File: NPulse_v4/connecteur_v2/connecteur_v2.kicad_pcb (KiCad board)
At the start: 4 copper layers, 39.8 x 51 mm, 26 parts, among them J1 Conn_01x02_Socket, J10 Conn_02x05_Odd_Even, J13 Conn_02x05_Odd_Even, J2 Conn_01x02_Socket, J23 Conn_01x01, J24 Conn_01x06_Socket, J25 Conn_01x06_Socket, J26 Conn_01x06_Socket, J27 Conn_01x01, J28 Conn_01x06_Socket, J29 Conn_01x06_Socket, J3 Conn_01x02_Socket, J30 Conn_01x06_Socket, J31 Conn_01x06_Socket, J32 Conn_02x05_Odd_Even, J33 Conn_01x06_Socket, J35 Conn_02x05_Odd_Even, J4 Conn_01x02_Socket, J45 Conn_01x01, J5 Conn_01x02_Socket, J54 Conn_02x05_Odd_Even, J57 Conn_02x05_Odd_Even, J6 Conn_01x04_Socket

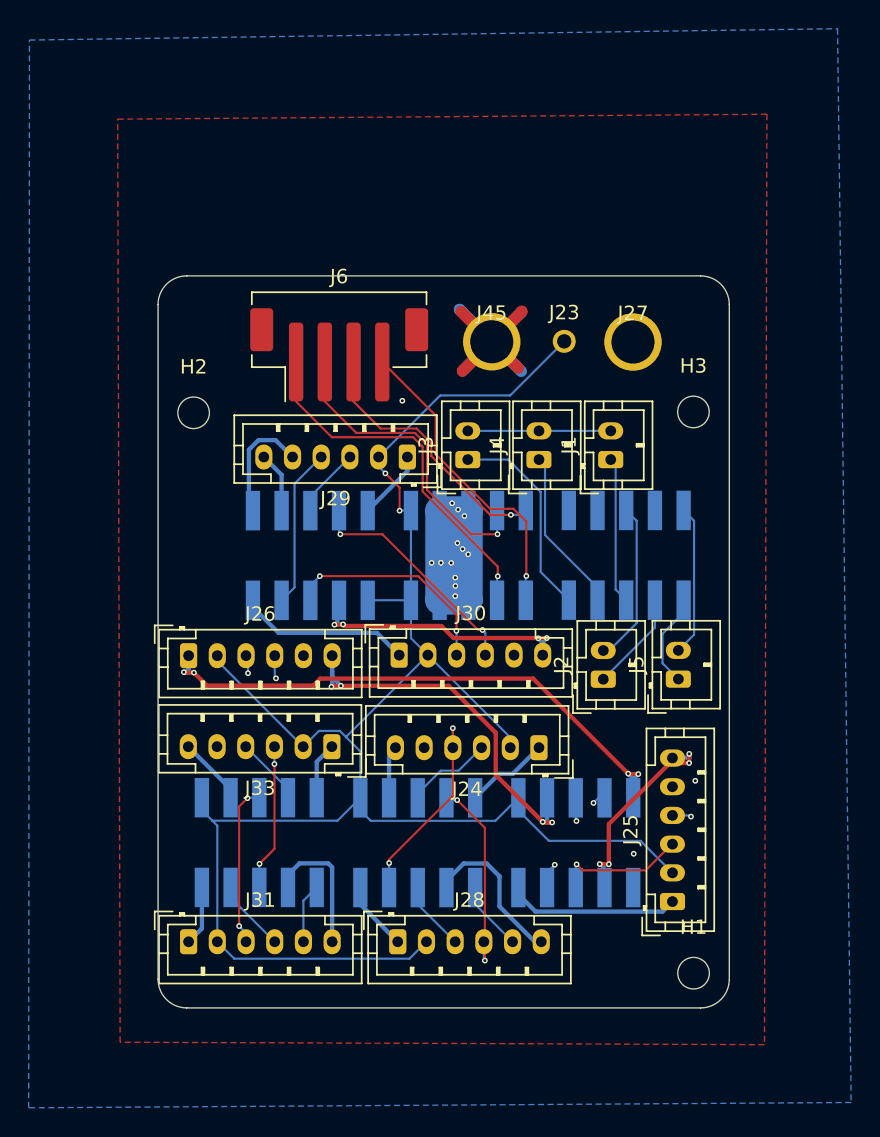
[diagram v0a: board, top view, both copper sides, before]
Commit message: add text on hat board, generate gerbers
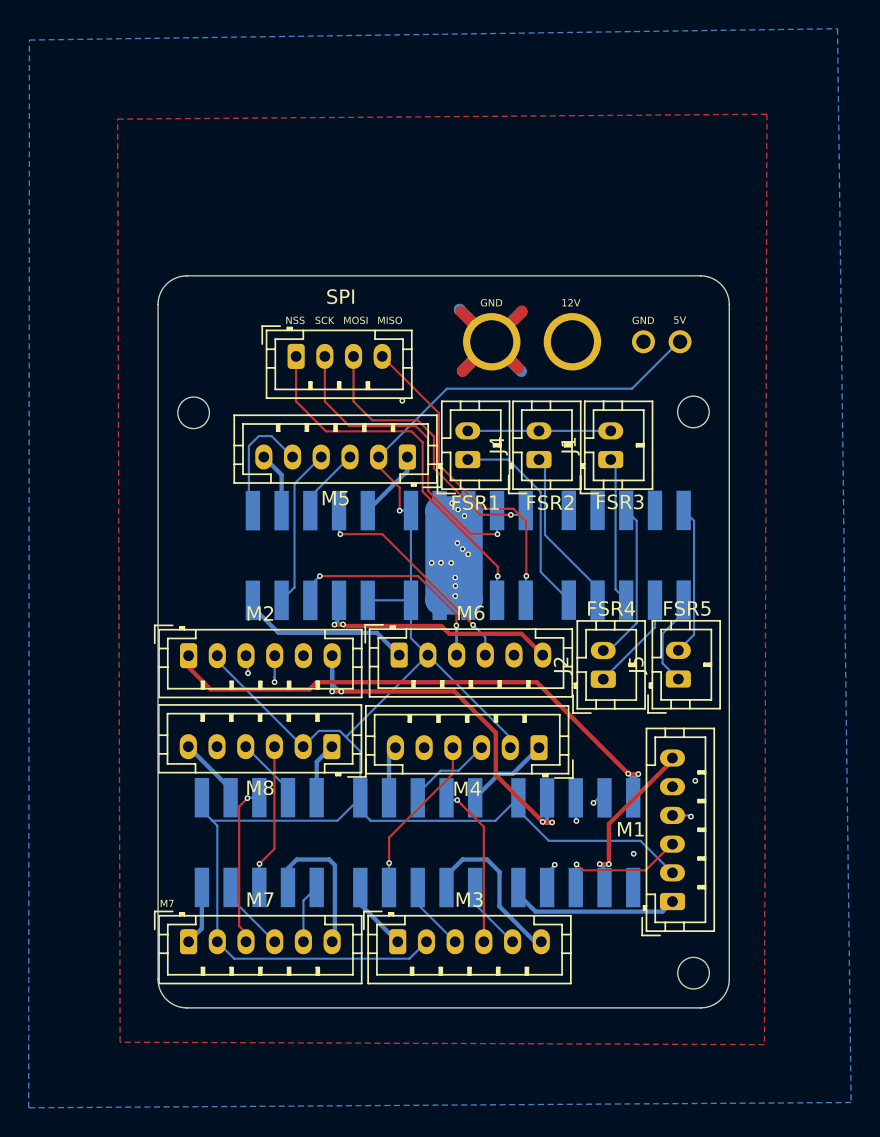
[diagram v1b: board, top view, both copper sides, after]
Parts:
- added ?: , , F.Cu at (187.2, 91.2)
- J6: footprint Connector_JST:JST_PH_B4B-PH-SM4-TB_1x04-1MP_P2.00mm_Vertical -> Connector_JST:JST_PH_B4B-PH-K_1x04_P2.00mm_Vertical
- moved J23 8.07 mm to (189.8, 91.2)
- moved J27 4.22 mm to (182.2, 91.2)
- moved J6 3.00 mm to (163.0, 92.2)
- renumbered J25 to M1, J26 to M2, J28 to M3, J24 to M4, J29 to M5, J30 to M6, J31 to M7, J33 to M8
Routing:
- net +5V: track 132.2 -> 141.0 mm, vias 2 -> 1
- net M1_1: track 15.6 -> 12.2 mm, vias 4 -> 2
- net ENC4_S1: track 14.3 -> 11.6 mm, vias 2 -> 1
- net ENC3_S1: track 14.1 -> 11.4 mm, vias 2 -> 1
- net M6_1: track 20.2 -> 17.7 mm, vias 4 -> 2
- net /+12V: track 80.9 -> 79.4 mm
- net M2_2: track 40.6 -> 39.3 mm, vias 4 -> 2
- net MOSI: track 18.7 -> 19.8 mm
- net ENC2_S2: track 31.5 -> 32.5 mm
- net M7_1: track 9.58 -> 10.4 mm
- net SCK: track 22.1 -> 22.8 mm
- net MISO: track 21.7 -> 22.4 mm
- net M3_1: track 11.1 -> 11.7 mm
- net ENC7_S2: track 11.3 -> 11.9 mm, vias 2 -> 1
- net NSS: track 25.8 -> 26.3 mm
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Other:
- board text added: "12V"
- board text added: "5V"
- board text added: "FSR1"
- board text added: "FSR2"
- board text added: "FSR3"
- board text added: "FSR4"
- board text added: "FSR5"
- board text added: "GND"
- board text added: "M7"
- board text added: "MISO"
- board text added: "MOSI"
- board text added: "NSS"
- board text added: "SCK"
- board text added: "SPI"

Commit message: restructure files and change vias on hat to 0.45mm diam
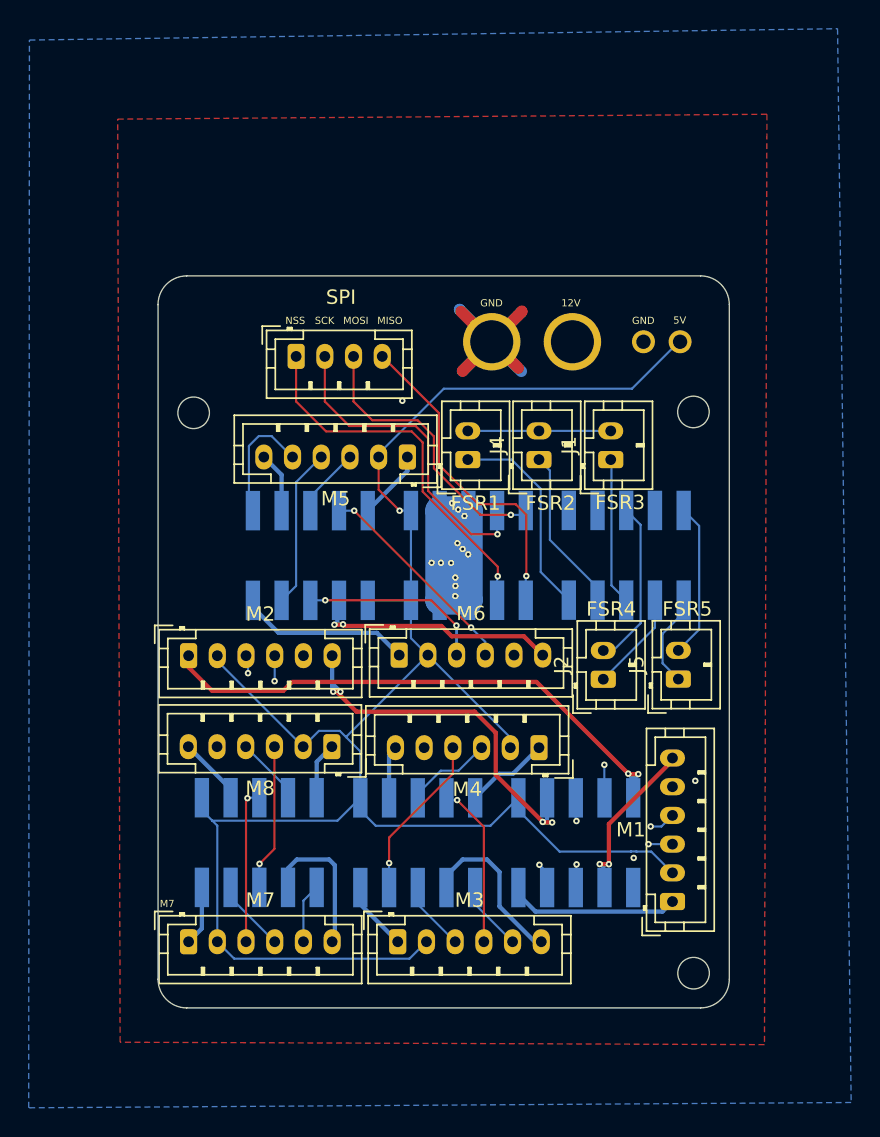
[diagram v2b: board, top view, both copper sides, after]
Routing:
- net ENC6_S2: track 15.4 -> 13.0 mm
- net ENC1_S1: track 11.1 -> 8.80 mm
- net ENC2_S1: track 28.4 -> 27.3 mm
- net ENC6_S1: track 16.0 -> 14.9 mm
- net ENC2_S2: track 32.5 -> 31.5 mm
- net M2_1: track 27.5 -> 26.7 mm
- net ENC1_S2: track 9.29 -> 9.47 mm, vias 1 -> 2
